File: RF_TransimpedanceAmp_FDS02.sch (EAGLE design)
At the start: 31 parts, among them IC1 PMA-5452, IC3 PMA-5452, IC4 ADM7150ARDZ-3.0, IC5 ADM7150ARDZ-5.0, X1 SMAJ502

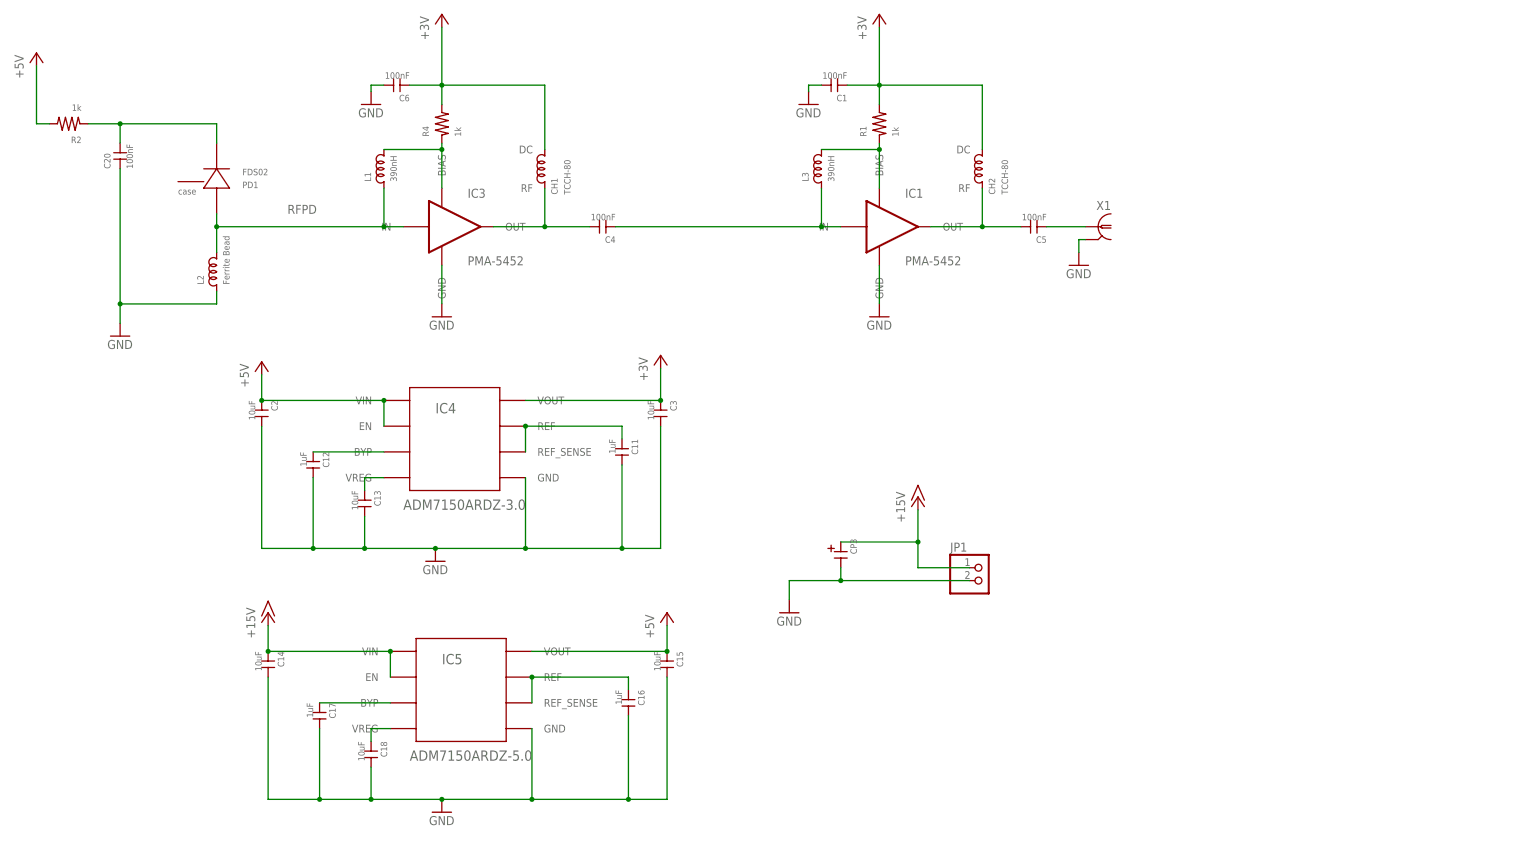
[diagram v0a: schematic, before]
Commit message: Added third stage amplifier, fixed layout issues.
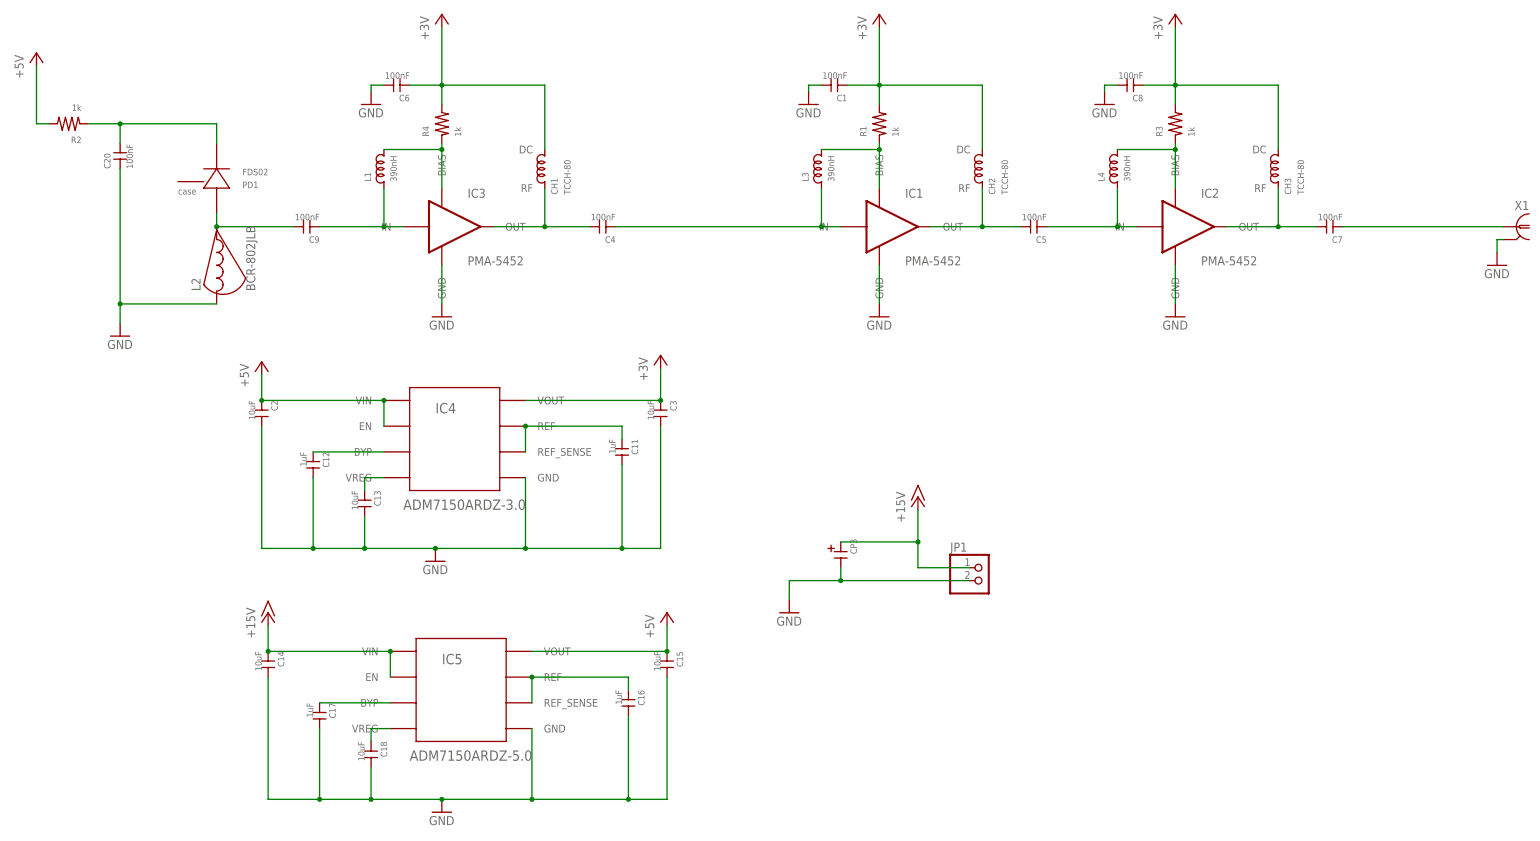
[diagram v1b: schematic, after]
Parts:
- added C7, C8, C9: 100nF, rlc-jqi:CAP0402
- added CH3: TCCH-80, rf-jqi:TCCH-80
- added IC2: PMA-5452, rf-jqi:PMA-5452
- added L4: 390nH, rlc-jqi:INDUCTOR-0402
- added R3: 1k, rlc-jqi:RES0402
- L2: value Ferrite Bead -> BCR-802JLB; device rlc-jqi:INDUCTOR-1206 -> coilcraft-jqi:BCR-802JLB; PARTNO 445-5223-1-ND -> (none)
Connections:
- new net N$10: IC2.BIAS, L4.P$2, R3.P$1
- new net N$4: C7.P$1, X1.1
- new net N$8: C7.P$2, CH3.RF, IC2.OUT
- new net RFPD2: C5.P$1, IC2.IN, L4.P$1
- net +3V: now also C8.P$1, CH3.DC, R3.P$2
- net GND: now also C8.P$2, IC2.GND, L2.2; no longer L2.P$1
- net N$7: now also C9.P$2, L2.1, PD1.ANODE; no longer C5.P$1, X1.1
- net RFPD: now also C9.P$1; no longer L2.P$2, PD1.ANODE
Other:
- moved on the sheet: X1
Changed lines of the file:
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@@
 <part name="PD1" library="semiconductor-jqi" deviceset="FDS02" device=""/>
 <part name="P+6" library="supply1" deviceset="+5V" device=""/>
-<part name="L2" library="rlc-jqi" deviceset="INDUCTOR" device="-1206" value="Ferrite Bead">
-<attribute name="PARTNO" value="445-5223-1-ND"/>
-</part>
 <part name="GND3" library="supply1" deviceset="GND" device=""/>
 <part name="R2" library="rlc-jqi" deviceset="RES" device="0402" value="1k"/>
@@
 <part name="GND6" library="supply1" deviceset="GND" device=""/>
 <part name="C4" library="rlc-jqi" deviceset="CAP" device="0402" value="100nF"/>
+<part name="C7" library="rlc-jqi" deviceset="CAP" device="0402" value="100nF"/>
+<part name="IC2" library="rf-jqi" deviceset="PMA-5452" device=""/>
+<part name="CH3" library="rf-jqi" deviceset="TCCH-80" device=""/>
+<part name="L4" library="rlc-jqi" deviceset="INDUCTOR" device="-0402" value="390nH"/>
+<part name="+3V3" library="supply1" deviceset="+3V3" device="" value="+3V"/>
+<part name="C8" library="rlc-jqi" deviceset="CAP" device="0402" value="100nF"/>
+<part name="GND7" library="supply1" deviceset="GND" device=""/>
+<part name="R3" library="rlc-jqi" deviceset="RES" device="0402" value="1k"/>
+<part name="GND8" library="supply1" deviceset="GND" device=""/>
+<part name="C9" library="rlc-jqi" deviceset="CAP" device="0402" value="100nF"/>
+<part name="L2" library="coilcraft-jqi" deviceset="BCR-802JLB" device=""/>
 </parts>
 <sheets>
@@
 <instance part="P+2" gate="1" x="20.32" y="34.29"/>
 <instance part="P+5" gate="1" x="19.05" y="83.82"/>
-<instance part="X1" gate="G$1" x="184.15" y="110.49" rot="MR0"/>
-<instance part="GND12" gate="1" x="180.34" y="102.87"/>
+<instance part="X1" gate="G$1" x="266.7" y="110.49" rot="MR0"/>
+<instance part="GND12" gate="1" x="262.89" y="102.87"/>
 <instance part="PD1" gate="G$1" x="10.16" y="121.92" rot="MR180"/>
 <instance part="P+6" gate="1" x="-25.4" y="144.78"/>
-<instance part="L2" gate="G$1" x="10.16" y="101.6" rot="R90">
-<attribute name="PARTNO" x="10.16" y="101.6" size="1.778" layer="96" display="off"/>
-</instance>
 <instance part="GND3" gate="1" x="-8.89" y="88.9"/>
 <instance part="R2" gate="G$1" x="-19.05" y="130.81" rot="R180"/>
@@
 <instance part="GND6" gate="1" x="140.97" y="92.71"/>
 <instance part="C4" gate="G$1" x="86.36" y="110.49" rot="R180"/>
+<instance part="C7" gate="G$1" x="229.87" y="110.49" rot="R180"/>
+<instance part="IC2" gate="G$1" x="199.39" y="110.49"/>
+<instance part="CH3" gate="G$1" x="219.71" y="121.92" rot="R90"/>
+<instance part="L4" gate="G$1" x="187.96" y="121.92" rot="R90"/>
+<instance part="+3V3" gate="G$1" x="199.39" y="152.4"/>
+<instance part="C8" gate="G$1" x="190.5" y="138.43" rot="R180"/>
+<instance part="GND7" gate="1" x="185.42" y="134.62"/>
+<instance part="R3" gate="G$1" x="199.39" y="130.81" rot="R90"/>
+<instance part="GND8" gate="1" x="199.39" y="92.71"/>
+<instance part="C9" gate="G$1" x="27.94" y="110.49" rot="R180"/>
+<instance part="L2" gate="G$1" x="10.16" y="102.87"/>
 </instances>
 <busses>
@@
 <pinref part="X1" gate="G$1" pin="2"/>
 <pinref part="GND12" gate="1" pin="GND"/>
-<wire x1="181.61" y1="107.95" x2="180.34" y2="107.95" width="0.1524" layer="91"/>
-<wire x1="180.34" y1="107.95" x2="180.34" y2="105.41" width="0.1524" layer="91"/>
+<wire x1="264.16" y1="107.95" x2="262.89" y2="107.95" width="0.1524" layer="91"/>
+<wire x1="262.89" y1="107.95" x2="262.89" y2="105.41" width="0.1524" layer="91"/>
 </segment>
 <segment>
@@
 <pinref part="GND3" gate="1" pin="GND"/>
 <wire x1="-8.89" y1="121.92" x2="-8.89" y2="95.25" width="0.1524" layer="91"/>
-<pinref part="L2" gate="G$1" pin="P$1"/>
 <wire x1="-8.89" y1="95.25" x2="-8.89" y2="91.44" width="0.1524" layer="91"/>
-<wire x1="10.16" y1="97.79" x2="10.16" y2="95.25" width="0.1524" layer="91"/>
 <wire x1="10.16" y1="95.25" x2="-8.89" y2="95.25" width="0.1524" layer="91"/>
 <junction x="-8.89" y="95.25"/>
+<pinref part="L2" gate="G$1" pin="2"/>
 </segment>
 <segment>
@@
 <pinref part="IC1" gate="G$1" pin="GND"/>
 <wire x1="140.97" y1="95.25" x2="140.97" y2="102.87" width="0.1524" layer="91"/>
+</segment>
+<segment>
+<pinref part="GND7" gate="1" pin="GND"/>
+<pinref part="C8" gate="G$1" pin="P$2"/>
+<wire x1="185.42" y1="137.16" x2="185.42" y2="138.43" width="0.1524" layer="91"/>
+<wire x1="185.42" y1="138.43" x2="187.96" y2="138.43" width="0.1524" layer="91"/>
+</segment>
+<segment>
+<pinref part="GND8" gate="1" pin="GND"/>
+<pinref part="IC2" gate="G$1" pin="GND"/>
+<wire x1="199.39" y1="95.25" x2="199.39" y2="102.87" width="0.1524" layer="91"/>
 </segment>
 </net>
@@
 <junction x="74.93" y="110.49"/>
 <pinref part="C4" gate="G$1" pin="P$2"/>
-</segment>
-</net>
-<net name="N$7" class="0">
-<segment>
-<pinref part="C5" gate="G$1" pin="P$1"/>
-<wire x1="173.99" y1="110.49" x2="181.61" y2="110.49" width="0.1524" layer="91"/>
-<pinref part="X1" gate="G$1" pin="1"/>
 </segment>
 </net>
@@
 <wire x1="140.97" y1="138.43" x2="161.29" y2="138.43" width="0.1524" layer="91"/>
 </segment>
+<segment>
+<pinref part="+3V3" gate="G$1" pin="+3V3"/>
+<pinref part="R3" gate="G$1" pin="P$2"/>
+<wire x1="199.39" y1="134.62" x2="199.39" y2="138.43" width="0.1524" layer="91"/>
+<pinref part="C8" gate="G$1" pin="P$1"/>
+<wire x1="199.39" y1="138.43" x2="199.39" y2="149.86" width="0.1524" layer="91"/>
+<wire x1="193.04" y1="138.43" x2="199.39" y2="138.43" width="0.1524" layer="91"/>
+<junction x="199.39" y="138.43"/>
+<pinref part="CH3" gate="G$1" pin="DC"/>
+<wire x1="219.71" y1="138.43" x2="219.71" y2="125.73" width="0.1524" layer="91"/>
+<wire x1="199.39" y1="138.43" x2="219.71" y2="138.43" width="0.1524" layer="91"/>
+</segment>
 </net>
 <net name="N$9" class="0">
@@
 <wire x1="43.18" y1="110.49" x2="46.99" y2="110.49" width="0.1524" layer="91"/>
 <wire x1="43.18" y1="118.11" x2="43.18" y2="110.49" width="0.1524" layer="91"/>
+<pinref part="C9" gate="G$1" pin="P$1"/>
+<wire x1="30.48" y1="110.49" x2="43.18" y2="110.49" width="0.1524" layer="91"/>
 <junction x="43.18" y="110.49"/>
-<label x="24.13" y="113.03" size="1.778" layer="95"/>
-<pinref part="PD1" gate="G$1" pin="ANODE"/>
-<wire x1="10.16" y1="113.03" x2="10.16" y2="110.49" width="0.1524" layer="91"/>
-<wire x1="10.16" y1="110.49" x2="43.18" y2="110.49" width="0.1524" layer="91"/>
-<pinref part="L2" gate="G$1" pin="P$2"/>
-<wire x1="10.16" y1="105.41" x2="10.16" y2="110.49" width="0.1524" layer="91"/>
-<junction x="10.16" y="110.49"/>
 </segment>
 </net>
@@
 </segment>
 </net>
+<net name="N$8" class="0">
+<segment>
+<pinref part="IC2" gate="G$1" pin="OUT"/>
+<wire x1="209.55" y1="110.49" x2="219.71" y2="110.49" width="0.1524" layer="91"/>
+<pinref part="CH3" gate="G$1" pin="RF"/>
+<wire x1="219.71" y1="118.11" x2="219.71" y2="110.49" width="0.1524" layer="91"/>
+<pinref part="C7" gate="G$1" pin="P$2"/>
+<wire x1="219.71" y1="110.49" x2="227.33" y2="110.49" width="0.1524" layer="91"/>
+<junction x="219.71" y="110.49"/>
+</segment>
+</net>
+<net name="N$10" class="0">
+<segment>
+<pinref part="L4" gate="G$1" pin="P$2"/>
+<pinref part="R3" gate="G$1" pin="P$1"/>
+<wire x1="187.96" y1="125.73" x2="199.39" y2="125.73" width="0.1524" layer="91"/>
+<wire x1="199.39" y1="125.73" x2="199.39" y2="127" width="0.1524" layer="91"/>
+<pinref part="IC2" gate="G$1" pin="BIAS"/>
+<wire x1="199.39" y1="125.73" x2="199.39" y2="118.11" width="0.1524" layer="91"/>
+<junction x="199.39" y="125.73"/>
+</segment>
+</net>
+<net name="RFPD2" class="0">
+<segment>
+<pinref part="IC2" gate="G$1" pin="IN"/>
+<pinref part="L4" gate="G$1" pin="P$1"/>
+<wire x1="187.96" y1="110.49" x2="191.77" y2="110.49" width="0.1524" layer="91"/>
+<wire x1="187.96" y1="118.11" x2="187.96" y2="110.49" width="0.1524" layer="91"/>
+<pinref part="C5" gate="G$1" pin="P$1"/>
+<wire x1="173.99" y1="110.49" x2="187.96" y2="110.49" width="0.1524" layer="91"/>
+<junction x="187.96" y="110.49"/>
+</segment>
+</net>
+<net name="N$4" class="0">
+<segment>
+<pinref part="C7" gate="G$1" pin="P$1"/>
+<pinref part="X1" gate="G$1" pin="1"/>
+<wire x1="232.41" y1="110.49" x2="264.16" y2="110.49" width="0.1524" layer="91"/>
+</segment>
+</net>
+<net name="N$7" class="0">
+<segment>
+<pinref part="PD1" gate="G$1" pin="ANODE"/>
+<wire x1="10.16" y1="113.03" x2="10.16" y2="110.49" width="0.1524" layer="91"/>
+<pinref part="C9" gate="G$1" pin="P$2"/>
+<wire x1="25.4" y1="110.49" x2="10.16" y2="110.49" width="0.1524" layer="91"/>
+<pinref part="L2" gate="G$1" pin="1"/>
+<junction x="10.16" y="110.49"/>
+</segment>
+</net>

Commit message: Misc store point; pushing for work at home
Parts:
- C13, C14, C15, C18, C2, C3: device rlc-jqi:CAP1210 -> rlc-jqi:CAP0805; PARTNO (none) -> 1276-2890-1-ND
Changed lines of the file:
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@@
 <?xml version="1.0" encoding="utf-8"?>
 <!DOCTYPE eagle SYSTEM "eagle.dtd">
-<eagle version="6.5.0">
+<eagle version="6.2">
 <drawing>
 <settings>
@@
 <setting verticaltext="up"/>
 </settings>
-<grid distance="0.05" unitdist="inch" unit="inch" style="lines" multiple="1" display="no" altdistance="0.01" altunitdist="inch" altunit="inch"/>
+<grid distance="0.1" unitdist="inch" unit="inch" style="lines" multiple="1" display="no" altdistance="0.01" altunitdist="inch" altunit="inch"/>
 <layers>
 <layer number="1" name="Top" color="4" fill="1" visible="no" active="no"/>
@@
 <part name="CP3" library="rlc-jqi" deviceset="CAP-POL" device="PANASONIC_F"/>
 <part name="IC4" library="regulator-jqi" deviceset="ADM7150" device="" value="ADM7150ARDZ-3.0"/>
-<part name="C2" library="rlc-jqi" deviceset="CAP" device="1210" value="10uF"/>
-<part name="C3" library="rlc-jqi" deviceset="CAP" device="1210" value="10uF"/>
+<part name="C2" library="rlc-jqi" deviceset="CAP" device="0805" value="10uF">
+<attribute name="PARTNO" value="1276-2890-1-ND"/>
+</part>
+<part name="C3" library="rlc-jqi" deviceset="CAP" device="0805" value="10uF">
+<attribute name="PARTNO" value="1276-2890-1-ND"/>
+</part>
 <part name="C11" library="rlc-jqi" deviceset="CAP" device="0402" value="1uF"/>
 <part name="C12" library="rlc-jqi" deviceset="CAP" device="0402" value="1uF"/>
-<part name="C13" library="rlc-jqi" deviceset="CAP" device="1210" value="10uF"/>
+<part name="C13" library="rlc-jqi" deviceset="CAP" device="0805" value="10uF">
+<attribute name="PARTNO" value="1276-2890-1-ND"/>
+</part>
 <part name="GND1" library="supply1" deviceset="GND" device=""/>
 <part name="IC5" library="regulator-jqi" deviceset="ADM7150" device="" value="ADM7150ARDZ-5.0"/>
-<part name="C14" library="rlc-jqi" deviceset="CAP" device="1210" value="10uF"/>
-<part name="C15" library="rlc-jqi" deviceset="CAP" device="1210" value="10uF"/>
+<part name="C14" library="rlc-jqi" deviceset="CAP" device="0805" value="10uF">
+<attribute name="PARTNO" value="1276-2890-1-ND"/>
+</part>
+<part name="C15" library="rlc-jqi" deviceset="CAP" device="0805" value="10uF">
+<attribute name="PARTNO" value="1276-2890-1-ND"/>
+</part>
 <part name="C16" library="rlc-jqi" deviceset="CAP" device="0402" value="1uF"/>
 <part name="C17" library="rlc-jqi" deviceset="CAP" device="0402" value="1uF"/>
-<part name="C18" library="rlc-jqi" deviceset="CAP" device="1210" value="10uF"/>
+<part name="C18" library="rlc-jqi" deviceset="CAP" device="0805" value="10uF">
+<attribute name="PARTNO" value="1276-2890-1-ND"/>
+</part>
 <part name="GND9" library="supply1" deviceset="GND" device=""/>
 <part name="+3V1" library="supply1" deviceset="+3V3" device="" value="+3V"/>
@@
 <attribute name="VALUE" x="46.99" y="54.61" size="2.032" layer="95"/>
 </instance>
-<instance part="C2" gate="G$1" x="19.05" y="73.66" rot="R270"/>
-<instance part="C3" gate="G$1" x="97.79" y="73.66" rot="R270"/>
+<instance part="C2" gate="G$1" x="19.05" y="73.66" rot="R270">
+<attribute name="PARTNO" x="19.05" y="73.66" size="1.778" layer="96" display="off"/>
+</instance>
+<instance part="C3" gate="G$1" x="97.79" y="73.66" rot="R270">
+<attribute name="PARTNO" x="97.79" y="73.66" size="1.778" layer="96" display="off"/>
+</instance>
 <instance part="C11" gate="G$1" x="90.17" y="66.04" rot="R270"/>
 <instance part="C12" gate="G$1" x="29.21" y="63.5" rot="R270"/>
-<instance part="C13" gate="G$1" x="39.37" y="55.88" rot="R270"/>
+<instance part="C13" gate="G$1" x="39.37" y="55.88" rot="R270">
+<attribute name="PARTNO" x="39.37" y="55.88" size="1.778" layer="96" display="off"/>
+</instance>
 <instance part="GND1" gate="1" x="53.34" y="44.45"/>
 <instance part="IC5" gate="G$1" x="57.15" y="16.51" smashed="yes">
@@
 <attribute name="VALUE" x="48.26" y="5.08" size="2.032" layer="95"/>
 </instance>
-<instance part="C14" gate="G$1" x="20.32" y="24.13" rot="R270"/>
-<instance part="C15" gate="G$1" x="99.06" y="24.13" rot="R270"/>
+<instance part="C14" gate="G$1" x="20.32" y="24.13" rot="R270">
+<attribute name="PARTNO" x="20.32" y="24.13" size="1.778" layer="96" display="off"/>
+</instance>
+<instance part="C15" gate="G$1" x="99.06" y="24.13" rot="R270">
+<attribute name="PARTNO" x="99.06" y="24.13" size="1.778" layer="96" display="off"/>
+</instance>
 <instance part="C16" gate="G$1" x="91.44" y="16.51" rot="R270"/>
 <instance part="C17" gate="G$1" x="30.48" y="13.97" rot="R270"/>
-<instance part="C18" gate="G$1" x="40.64" y="6.35" rot="R270"/>
+<instance part="C18" gate="G$1" x="40.64" y="6.35" rot="R270">
+<attribute name="PARTNO" x="40.64" y="6.35" size="1.778" layer="96" display="off"/>
+</instance>
 <instance part="GND9" gate="1" x="54.61" y="-5.08"/>
 <instance part="+3V1" gate="G$1" x="97.79" y="85.09"/>
